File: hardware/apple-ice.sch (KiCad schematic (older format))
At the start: 77 parts, among them J1 TO_SP_DRIVE, J2 USB_B_Micro, J3 SPI_FLASH_PROG, P1 A2Bus-apple2, SW1 SW_Push, SW2 SW_Push, SW3 SW_Push, U1 SN74LVC8T245PW, U10 W25Q16JVSS, U2 SN74LVC8T245PW, U3 SN74LVC8T245PW, U4 SN74LVC8T245PW, U5 SN74LVC8T245PW, U6 ICE40HX1K-TQ144, U7 SN74LVC8T245PW, U8 MCP1703A-3302_SOT223, U9 MCP1703A-1202_SOT223, X1 ECS-2520MV-xxx-xx

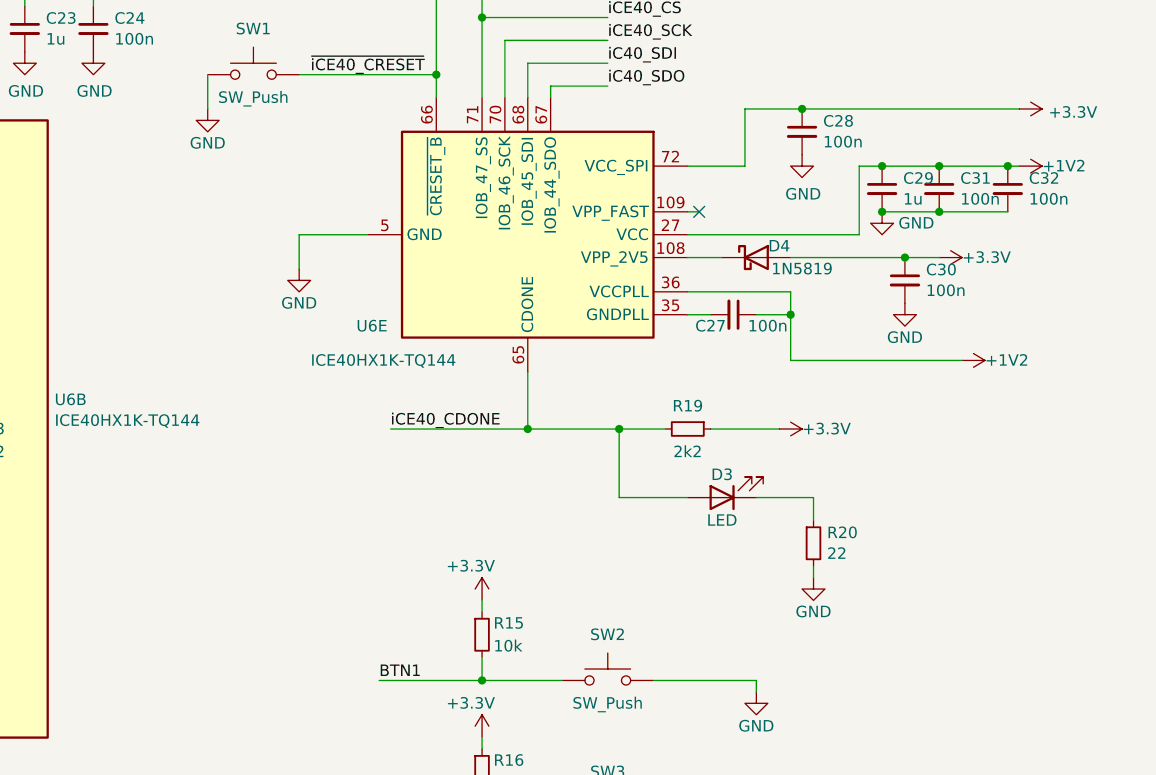
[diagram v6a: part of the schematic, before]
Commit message: Add new micro USB footprint
Signed-off-by: Rangel Ivanov <rangelivanov88@gmail.com>
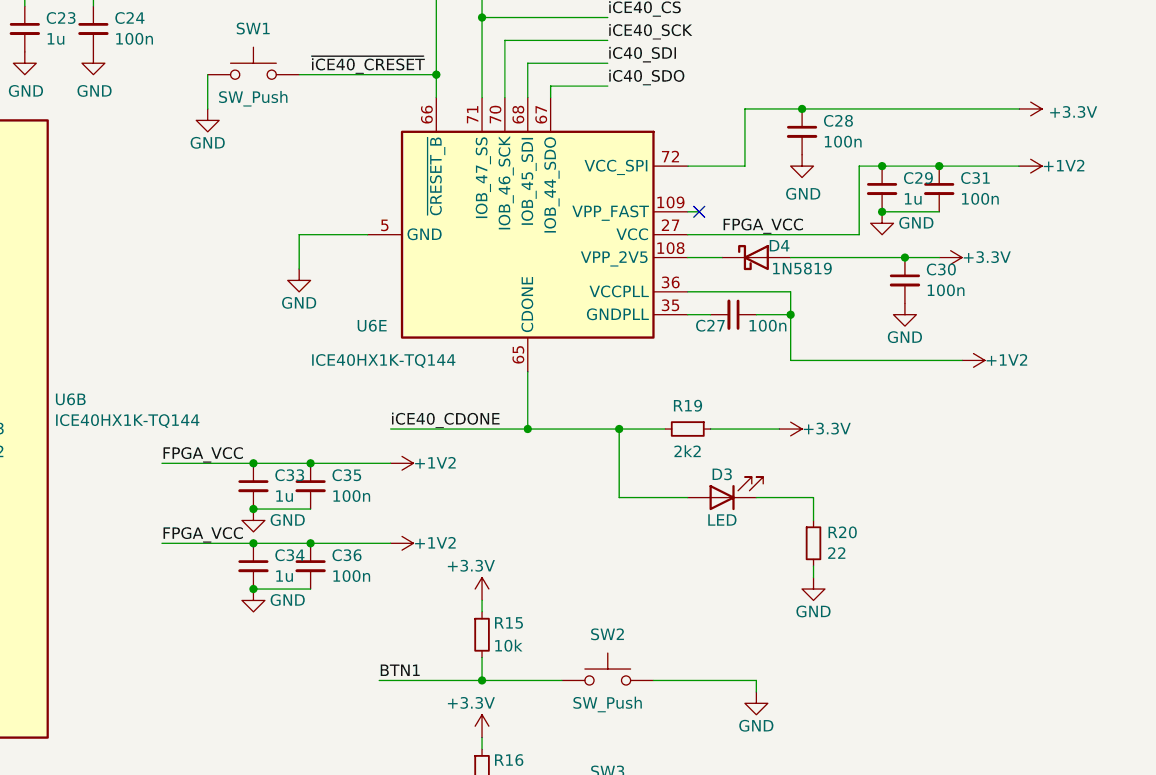
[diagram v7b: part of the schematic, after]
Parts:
- removed C32: 100n, apple-ice:C_0603_1608Metric_Pad1.08x0.95mm_HandSolder, symbol apple-ice:C_Small
- added C33, C34: 1u, apple-ice:C_0603_1608Metric_Pad1.08x0.95mm_HandSolder, symbol apple-ice:C_Small
- added C35, C36: 100n, apple-ice:C_0603_1608Metric_Pad1.08x0.95mm_HandSolder, symbol apple-ice:C_Small
- J2: footprint apple-ice:USB_Micro-B_Molex-105017-0001 -> apple-ice:MOLEX-0475890001
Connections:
- net +1V2: now also C33.1, C34.1, C35.1, C36.1
- net GND: now also C33.2, C34.2, C35.2, C36.2
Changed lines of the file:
@@
 Connection ~ 15250 4800
-Wire Wire Line
-	15250 4800 15550 4800
 Wire Wire Line
 	14900 5100 14900 4800
@@
 F 0 "J2" H 11607 9817 50  0000 C CNN
 F 1 "USB_B_Micro" H 11607 9726 50  0000 C CNN
-F 2 "apple-ice:USB_Micro-B_Molex-105017-0001" H 11700 9300 50  0001 C CNN
-F 3 "~" H 11700 9300 50  0001 C CNN
+F 2 "apple-ice:MOLEX-0475890001" H 11700 9300 50  0001 C CNN
+F 3 "https://store.comet.bg/Catalogue/Product/21020/" H 11700 9300 50  0001 C CNN
 	1    11550 9350
 	1    0    0    -1
@@
 Wire Wire Line
 	9850 6150 10500 6150
-$Comp
-L apple-ice:C_Small C32
-U 1 1 68DD6B05
-P 15550 4900
-F 0 "C32" H 15642 4946 50  0000 L CNN
-F 1 "100n" H 15642 4855 50  0000 L CNN
-F 2 "apple-ice:C_0603_1608Metric_Pad1.08x0.95mm_HandSolder" H 15550 4900 50  0001 C CNN
-F 3 "~" H 15550 4900 50  0001 C CNN
-	1    15550 4900
-	1    0    0    -1
-$EndComp
-Connection ~ 15550 4800
-Wire Wire Line
-	15550 4800 15600 4800
-Wire Wire Line
-	15250 5000 15550 5000
-Connection ~ 15250 5000
 $Comp
 L apple-ice:R_Small R10
@@
 NoConn ~ 10500 4950
 NoConn ~ 10500 5050
+Text Label 14300 5100 0    50   ~ 0
+FPGA_VCC
+$Comp
+L apple-ice:+1V2 #PWR03
+U 1 1 60EA4B41
+P 12850 6100
+F 0 "#PWR03" H 12850 5950 50  0001 C CNN
+F 1 "+1V2" V 12850 6200 50  0000 L CNN
+F 2 "" H 12850 6100 50  0001 C CNN
+F 3 "" H 12850 6100 50  0001 C CNN
+	1    12850 6100
+	0    1    1    0
+$EndComp
+$Comp
+L apple-ice:C_Small C35
+U 1 1 60EA4B48
+P 12500 6200
+F 0 "C35" H 12592 6246 50  0000 L CNN
+F 1 "100n" H 12592 6155 50  0000 L CNN
+F 2 "apple-ice:C_0603_1608Metric_Pad1.08x0.95mm_HandSolder" H 12500 6200 50  0001 C CNN
+F 3 "~" H 12500 6200 50  0001 C CNN
+	1    12500 6200
+	1    0    0    -1
+$EndComp
+Connection ~ 12500 6100
+$Comp
+L apple-ice:C_Small C33
+U 1 1 60EA4B50
+P 12250 6200
+F 0 "C33" H 12342 6246 50  0000 L CNN
+F 1 "1u" H 12342 6155 50  0000 L CNN
+F 2 "apple-ice:C_0603_1608Metric_Pad1.08x0.95mm_HandSolder" H 12250 6200 50  0001 C CNN
+F 3 "~" H 12250 6200 50  0001 C CNN
+	1    12250 6200
+	1    0    0    -1
+$EndComp
+Connection ~ 12250 6100
+Wire Wire Line
+	12250 6100 12500 6100
+$Comp
+L apple-ice:GND #PWR01
+U 1 1 60EA4B58
+P 12250 6300
+F 0 "#PWR01" H 12250 6050 50  0001 C CNN
+F 1 "GND" H 12400 6250 50  0000 C CNN
+F 2 "" H 12250 6300 50  0001 C CNN
+F 3 "" H 12250 6300 50  0001 C CNN
+	1    12250 6300
+	1    0    0    -1
+$EndComp
+Wire Wire Line
+	12500 6300 12250 6300
+Connection ~ 12250 6300
+Wire Wire Line
+	12500 6100 12850 6100
+$Comp
+L apple-ice:+1V2 #PWR04
+U 1 1 61027784
+P 12850 6450
+F 0 "#PWR04" H 12850 6300 50  0001 C CNN
+F 1 "+1V2" V 12850 6550 50  0000 L CNN
+F 2 "" H 12850 6450 50  0001 C CNN
+F 3 "" H 12850 6450 50  0001 C CNN
+	1    12850 6450
+	0    1    1    0
+$EndComp
+$Comp
+L apple-ice:C_Small C36
+U 1 1 6102778B
+P 12500 6550
+F 0 "C36" H 12592 6596 50  0000 L CNN
+F 1 "100n" H 12592 6505 50  0000 L CNN
+F 2 "apple-ice:C_0603_1608Metric_Pad1.08x0.95mm_HandSolder" H 12500 6550 50  0001 C CNN
+F 3 "~" H 12500 6550 50  0001 C CNN
+	1    12500 6550
+	1    0    0    -1
+$EndComp
+Connection ~ 12500 6450
+$Comp
+L apple-ice:C_Small C34
+U 1 1 61027792
+P 12250 6550
+F 0 "C34" H 12342 6596 50  0000 L CNN
+F 1 "1u" H 12342 6505 50  0000 L CNN
+F 2 "apple-ice:C_0603_1608Metric_Pad1.08x0.95mm_HandSolder" H 12250 6550 50  0001 C CNN
+F 3 "~" H 12250 6550 50  0001 C CNN
+	1    12250 6550
+	1    0    0    -1
+$EndComp
+Connection ~ 12250 6450
+Wire Wire Line
+	12250 6450 12500 6450
+$Comp
+L apple-ice:GND #PWR02
+U 1 1 6102779A
+P 12250 6650
+F 0 "#PWR02" H 12250 6400 50  0001 C CNN
+F 1 "GND" H 12400 6600 50  0000 C CNN
+F 2 "" H 12250 6650 50  0001 C CNN
+F 3 "" H 12250 6650 50  0001 C CNN
+	1    12250 6650
+	1    0    0    -1
+$EndComp
+Wire Wire Line
+	12500 6650 12250 6650
+Connection ~ 12250 6650
+Wire Wire Line
+	12500 6450 12850 6450
+Text Label 11850 6100 0    50   ~ 0
+FPGA_VCC
+Wire Wire Line
+	11850 6100 12250 6100
+Text Label 11850 6450 0    50   ~ 0
+FPGA_VCC
+Wire Wire Line
+	11850 6450 12250 6450
+Wire Wire Line
+	15250 4800 15600 4800
 Wire Bus Line
 	3700 9250 3700 10150

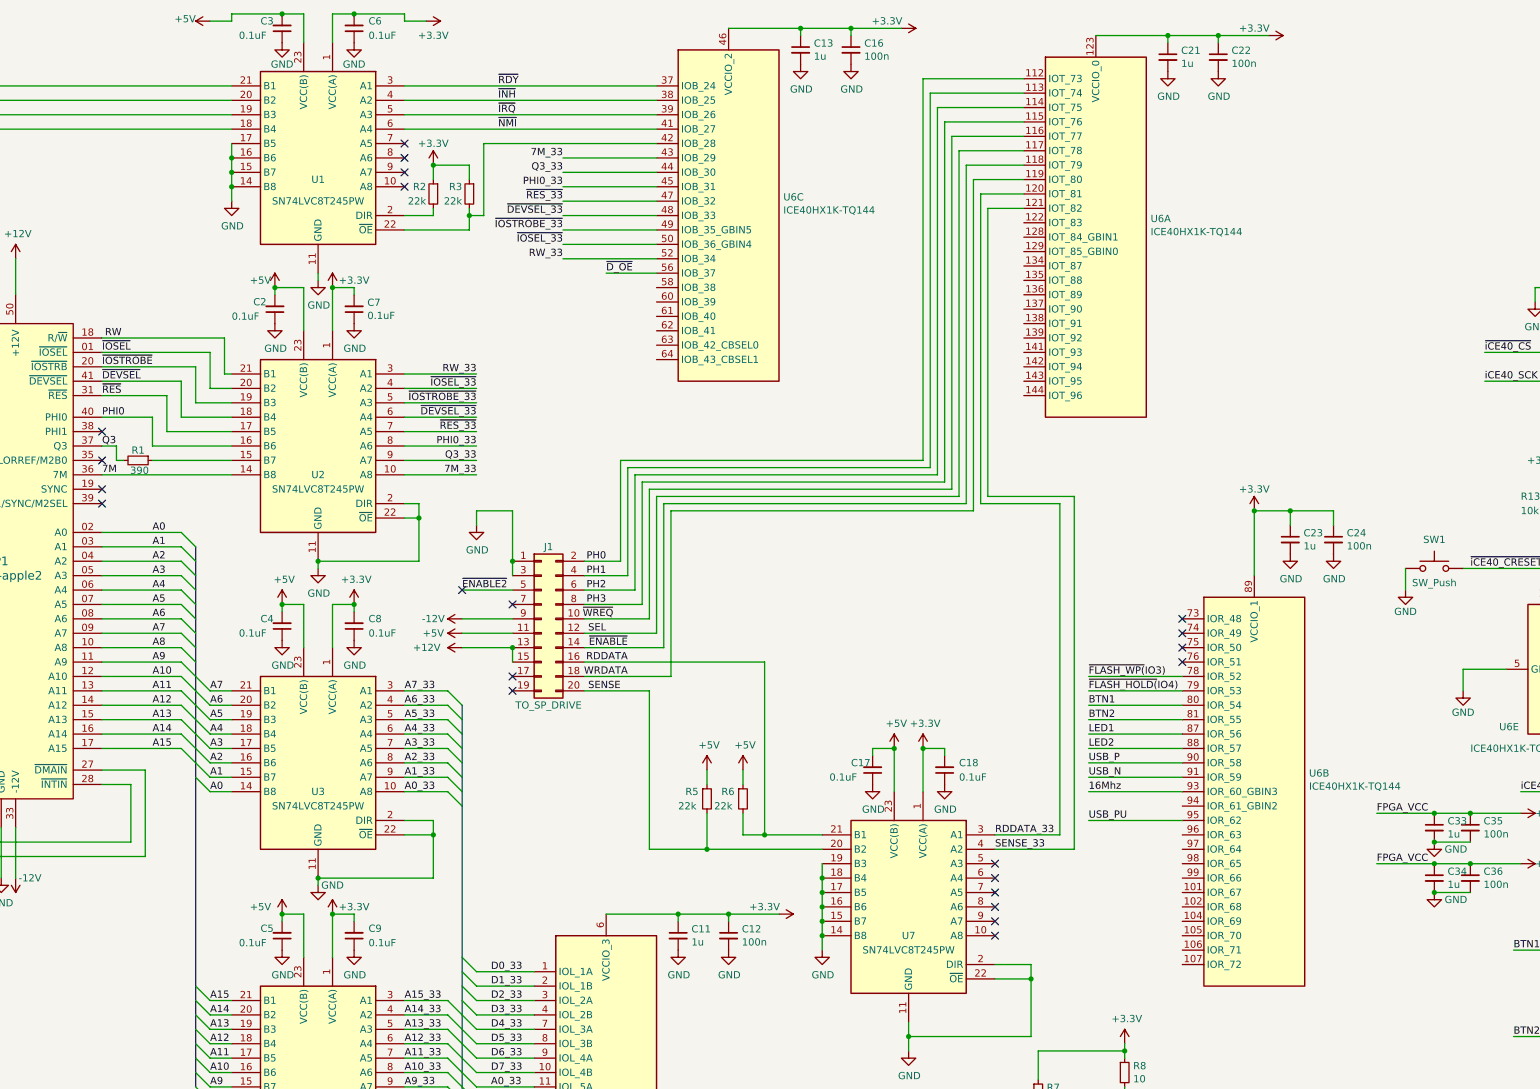
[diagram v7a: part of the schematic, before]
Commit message: More schematic tweaking for easier routing
Signed-off-by: Rangel Ivanov <rangelivanov88@gmail.com>
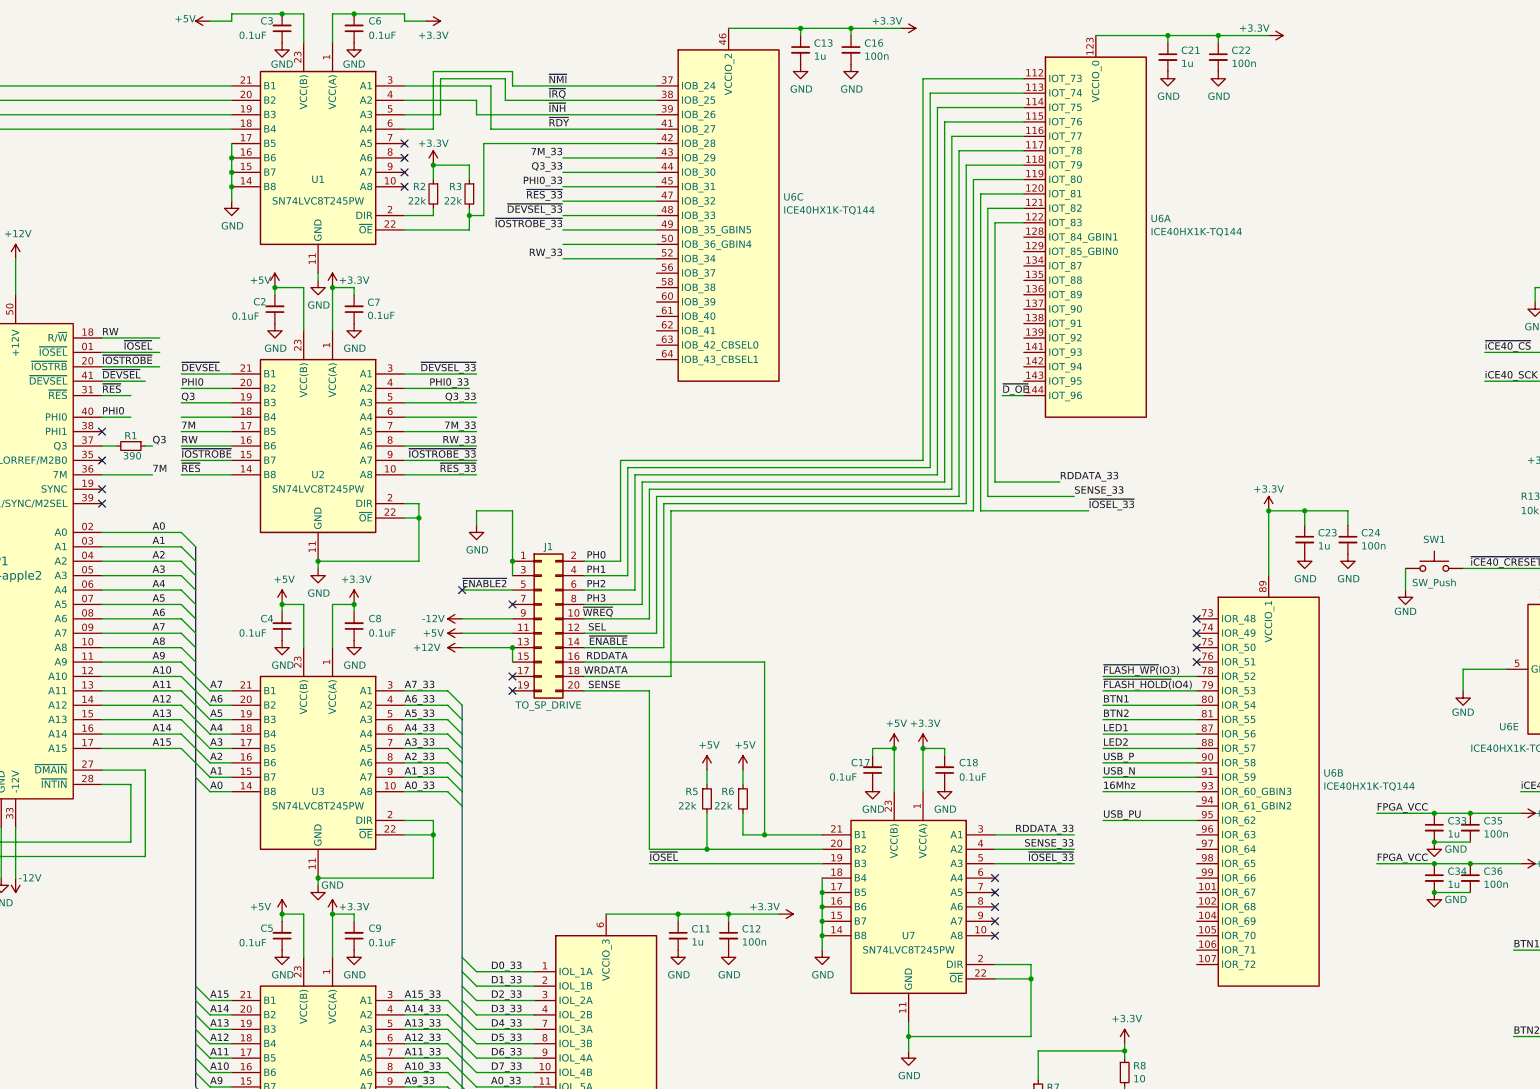
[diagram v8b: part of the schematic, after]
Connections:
- net 7M: now also U2.17 (B5); no longer U2.14 (B8)
- net 7M_33: now also U2.7 (A5); no longer U2.10 (A8)
- net GND: no longer U7.19 (B3)
- net PHI0: now also U2.20 (B2); no longer U2.16 (B6)
- net PHI0_33: now also U2.4 (A2); no longer U2.8 (A6)
- net Q3: now also R1.1, U2.19 (B3); no longer P1.37 (Q3), R1.2
- net Q3_33: now also U2.5 (A3); no longer U2.9 (A7)
- net RDDATA_33: now also U6.122 (IOT_83); no longer U6.120 (IOT_81)
- net RW: now also U2.16 (B6); no longer U2.21 (B1)
- net RW_33: now also U2.8 (A6); no longer U2.3 (A1)
- net ~DEVSEL: now also U2.21 (B1); no longer U2.18 (B4)
- net ~DEVSEL_33: now also U2.3 (A1); no longer U2.6 (A4)
- net ~D_OE: now also U6.144 (IOT_96); no longer U6.56 (IOB_37)
- net ~INH: now also U6.39 (IOB_26); no longer U6.38 (IOB_25)
- net ~IOSEL: now also U7.19 (B3); no longer U2.20 (B2)
- net ~IOSEL_33: now also U6.120 (IOT_81), U7.5 (A3); no longer U2.4 (A2), U6.50 (IOB_36_GBIN4)
- net ~IOSTROBE: now also U2.15 (B7); no longer U2.19 (B3)
- net ~IOSTROBE_33: now also U2.9 (A7); no longer U2.5 (A3)
- net ~IRQ: now also U6.38 (IOB_25); no longer U6.39 (IOB_26)
- net ~NMI: now also U6.37 (IOB_24); no longer U6.41 (IOB_27)
- net ~RDY: now also U6.41 (IOB_27); no longer U6.37 (IOB_24)
- net ~RES: now also U2.14 (B8); no longer U2.17 (B5)
- net ~RES_33: now also U2.10 (A8); no longer U2.7 (A5)
- new net: P1.37 (Q3), R1.2
- no-connect marks 29 -> 28
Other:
- moved on the sheet: C23, C24, R1, U6B
